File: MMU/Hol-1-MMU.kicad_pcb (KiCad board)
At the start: 2 copper layers, 106.7 x 76.2 mm, 0 parts

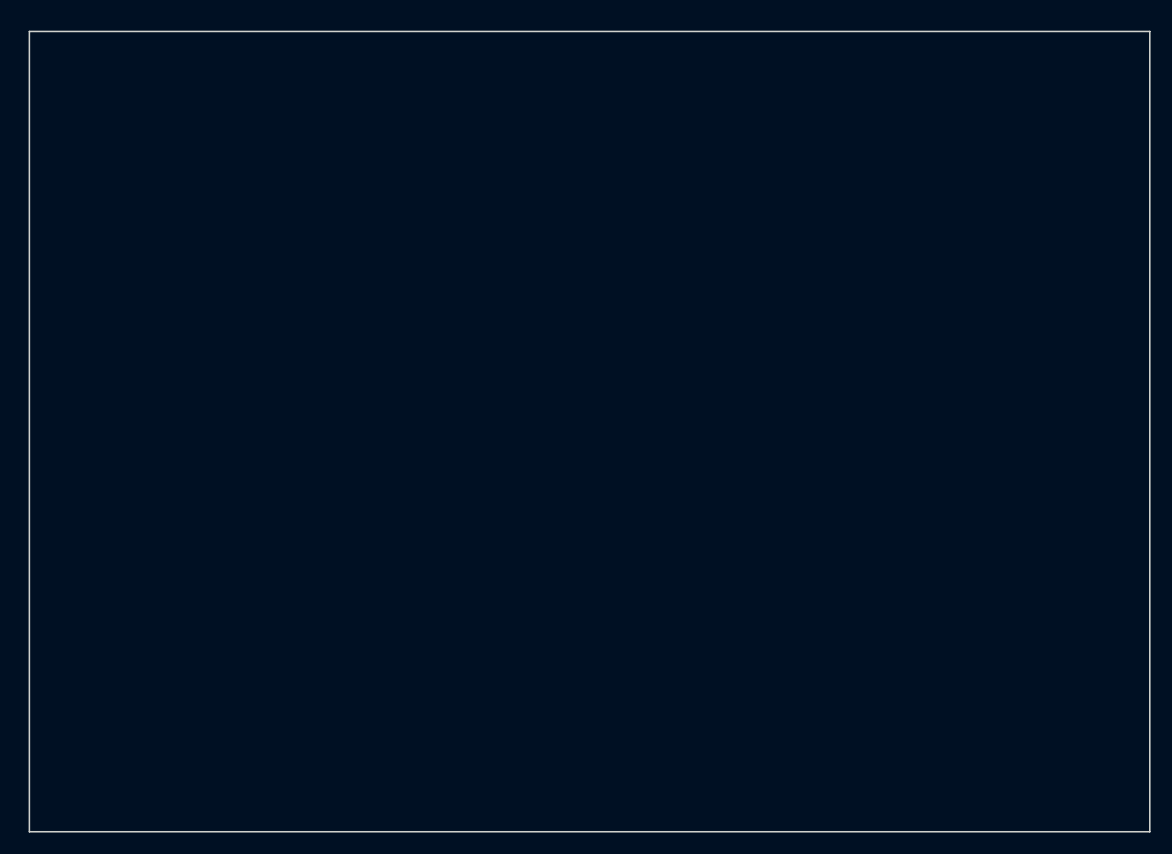
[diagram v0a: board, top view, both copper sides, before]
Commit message: v1.5.2 MMU power + blinkenlights added
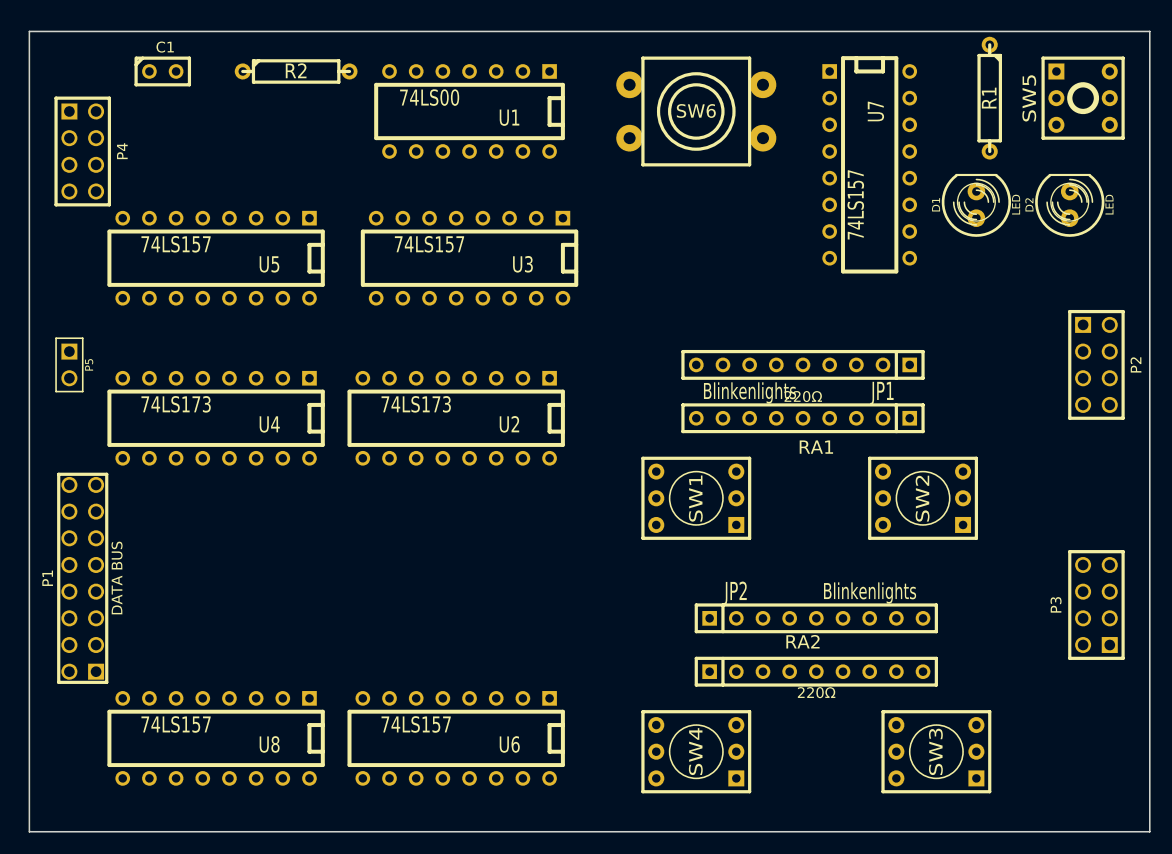
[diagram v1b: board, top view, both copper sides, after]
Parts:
- added C1: 0.01uF, C1, F.Cu at (116.8, 67.3)
- added D1: LED, LED-5MM, F.Cu at (194.3, 80.0)
- added D2: LED, LED-5MM, F.Cu at (203.2, 80.0)
- added JP1: Blinkenlights, SIL-9, F.Cu at (177.8, 95.2)
- added JP2: Blinkenlights, SIL-9, F.Cu at (179.1, 119.4)
- added P1: DATA BUS, pin_array_8x2, F.Cu at (109.2, 115.6)
- added P2: ADDRESS PORT, pin_array_4x2, F.Cu at (205.7, 95.2)
- added P3: DATA PORT, pin_array_4x2, F.Cu at (205.7, 118.1)
- added P4: MMU CONTROL, pin_array_4x2, F.Cu at (109.2, 74.9)
- added P5: Power, PIN_ARRAY_2X1, F.Cu at (108.0, 95.2)
- added R1: 220Ω, R4, F.Cu at (195.6, 69.8)
- added R2: 1K, R4, F.Cu at (129.5, 67.3)
- added RA1: 220Ω, r_pack8, F.Cu at (177.8, 100.3)
- added RA2: 220Ω, r_pack8, F.Cu at (179.1, 124.5)
- added SW1: HEX_SWITCH, SW_Hex6, F.Cu at (167.6, 108.0)
- added SW2: HEX_SWITCH, SW_Hex6, F.Cu at (189.2, 108.0)
- added SW3: HEX_SWITCH, SW_Hex6, F.Cu at (190.5, 132.1)
- added SW4: HEX_SWITCH, SW_Hex6, F.Cu at (167.6, 132.1)
- added SW5: DPDT, sw-dpdt-push, F.Cu at (204.5, 69.8)
- added SW6: SW_PUSH, sw_push_lrg, F.Cu at (167.6, 71.1)
- added U1: 74LS00, DIP-14, F.Cu at (146.1, 71.1)
- added U2: 74LS173, DIP-16, F.Cu at (144.8, 100.3)
- added U3: 74LS157, DIP-16, F.Cu at (146.1, 85.1)
- added U4: 74LS173, DIP-16, F.Cu at (121.9, 100.3)
- added U5: 74LS157, DIP-16, F.Cu at (121.9, 85.1)
- added U6: 74LS157, DIP-16, F.Cu at (144.8, 130.8)
- added U7: 74LS157, DIP-16, F.Cu at (184.2, 76.2)
- added U8: 74LS157, DIP-16, F.Cu at (121.9, 130.8)

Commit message: v1.5.3 initial MMU board layout
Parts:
- moved P2 79.1 mm to (130.8, 69.8), turned to 180 degrees
- moved SW5 58.8 mm to (172.7, 119.4), turned to 180 degrees
- moved D2 46.6 mm to (162.6, 102.9)
- moved R1 44.7 mm to (170.2, 106.7), turned to 0 degrees
- moved P3 44.5 mm to (161.3, 118.1)
- moved SW4 42.1 mm to (204.5, 111.8)
- moved SW1 40.4 mm to (204.5, 91.4)
- moved SW2 39.9 mm to (204.5, 71.1)
- moved D1 28.2 mm to (177.8, 102.9)
- moved RA1 22.5 mm to (193.0, 83.8), turned to 270 degrees
- moved U7 20.4 mm to (163.8, 74.9)
- moved RA2 14.9 mm to (193.0, 119.4), turned to 270 degrees
- moved SW3 14.0 mm to (204.5, 132.1)
- moved JP1 12.5 mm to (182.9, 83.8), turned to 270 degrees
- moved SW6 7.73 mm to (175.3, 72.4), turned to 270 degrees
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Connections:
- P4 pad 1: /RAM-INPUT -> (no net)
- P4 pad 2: /CLK -> (no net)
- P4 pad 4: (no net) -> /RAM-INPUT
- P4 pad 6: (no net) -> /CLK
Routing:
- net GND: track 0.00 -> 375.7 mm, vias 0 -> 15
- net +5V: track 0.00 -> 360.7 mm, vias 0 -> 8
- net /PROG: track 0.00 -> 162.3 mm, vias 0 -> 4
- net N-0000049: track 0.00 -> 119.5 mm, vias 0 -> 3
- net N-0000050: track 0.00 -> 117.9 mm, vias 0 -> 4
- net N-0000010: track 0.00 -> 110.3 mm, vias 0 -> 3
- net N-000006: track 0.00 -> 109.5 mm, vias 0 -> 2
- net N-0000056: track 0.00 -> 106.7 mm, vias 0 -> 1
- net N-000002: track 0.00 -> 102.7 mm
- net N-0000062: track 0.00 -> 99.4 mm, vias 0 -> 4
- net N-0000063: track 0.00 -> 92.0 mm, vias 0 -> 4
- net N-000003: track 0.00 -> 87.4 mm, vias 0 -> 1
- net N-000001: track 0.00 -> 79.0 mm, vias 0 -> 2
- net N-0000064: track 0.00 -> 78.0 mm, vias 0 -> 2
- net N-0000040: track 0.00 -> 78.0 mm, vias 0 -> 1
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
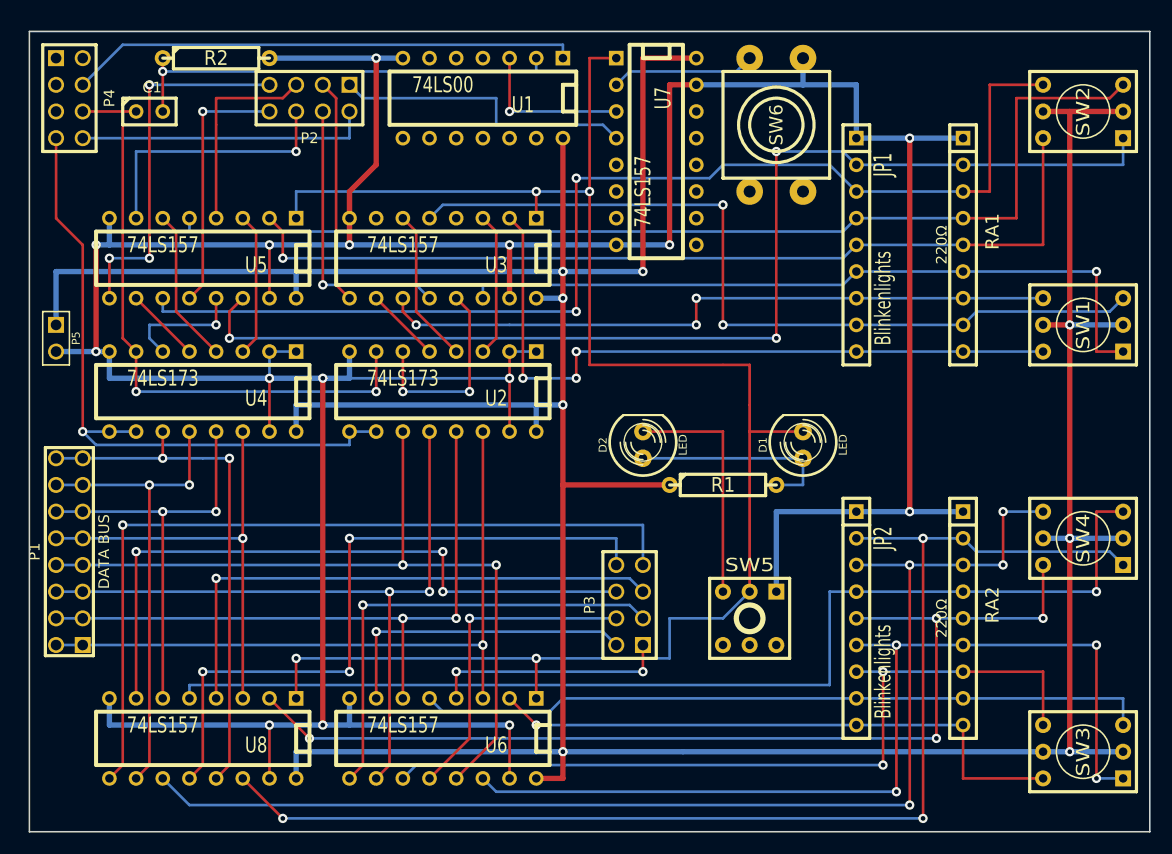
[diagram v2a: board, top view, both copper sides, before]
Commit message: v1.5.4 MMU add bypass caps
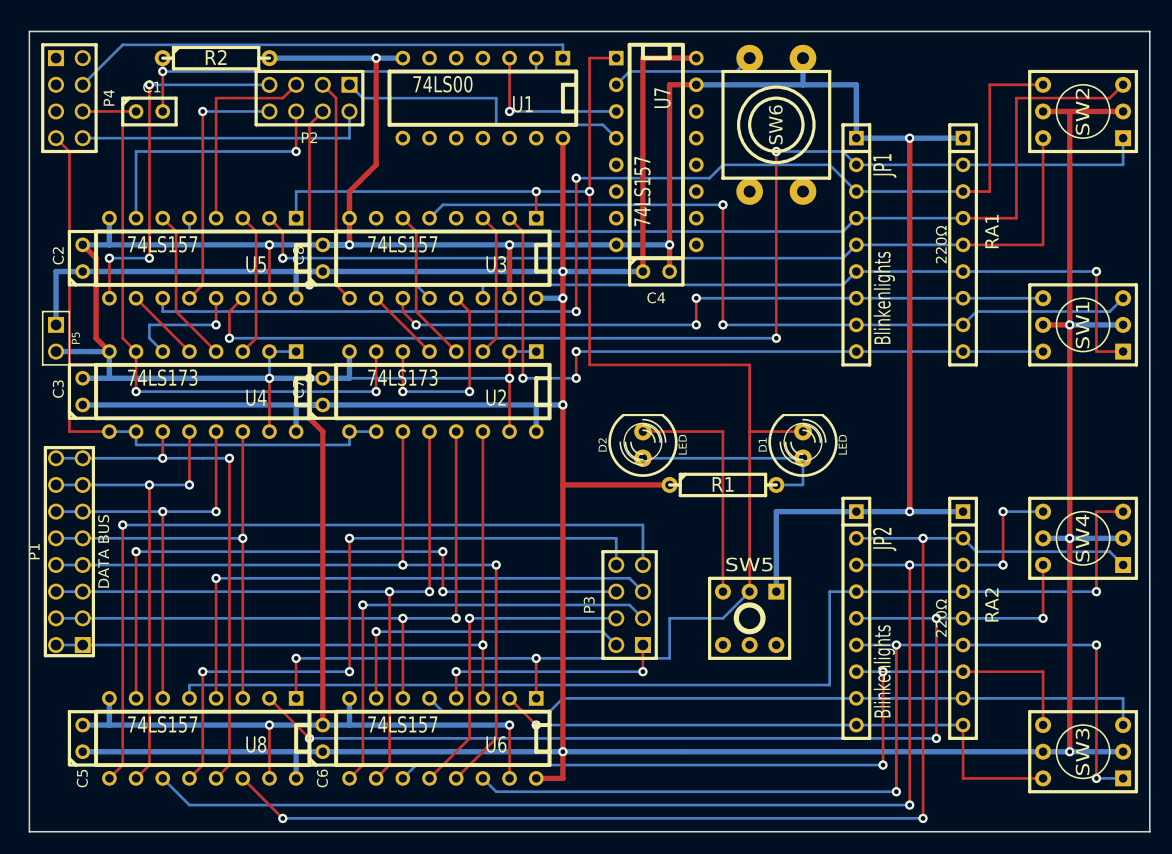
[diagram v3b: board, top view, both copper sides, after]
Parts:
- added C2: 100nF, C1, F.Cu at (109.2, 85.1)
- added C3: 100nF, C1, F.Cu at (109.2, 97.8)
- added C4: 100nF, C1, F.Cu at (163.8, 86.4)
- added C5: 100nF, C1, F.Cu at (109.2, 130.8)
- added C6: 100nF, C1, F.Cu at (132.1, 130.8)
- added C7: 100nF, C1, F.Cu at (132.1, 97.8)
- added C8: 100nF, C1, F.Cu at (132.1, 85.1)
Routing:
- net +5V: track 360.7 -> 405.1 mm, vias 8 -> 7
- net GND: track 375.7 -> 388.7 mm, vias 15 -> 12
- net /IN-D: track 63.8 -> 60.2 mm, vias 1 -> 0
- net N-0000018: track 27.2 -> 29.0 mm

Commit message: v1.5.5 MMU reduce vias and tidy-up
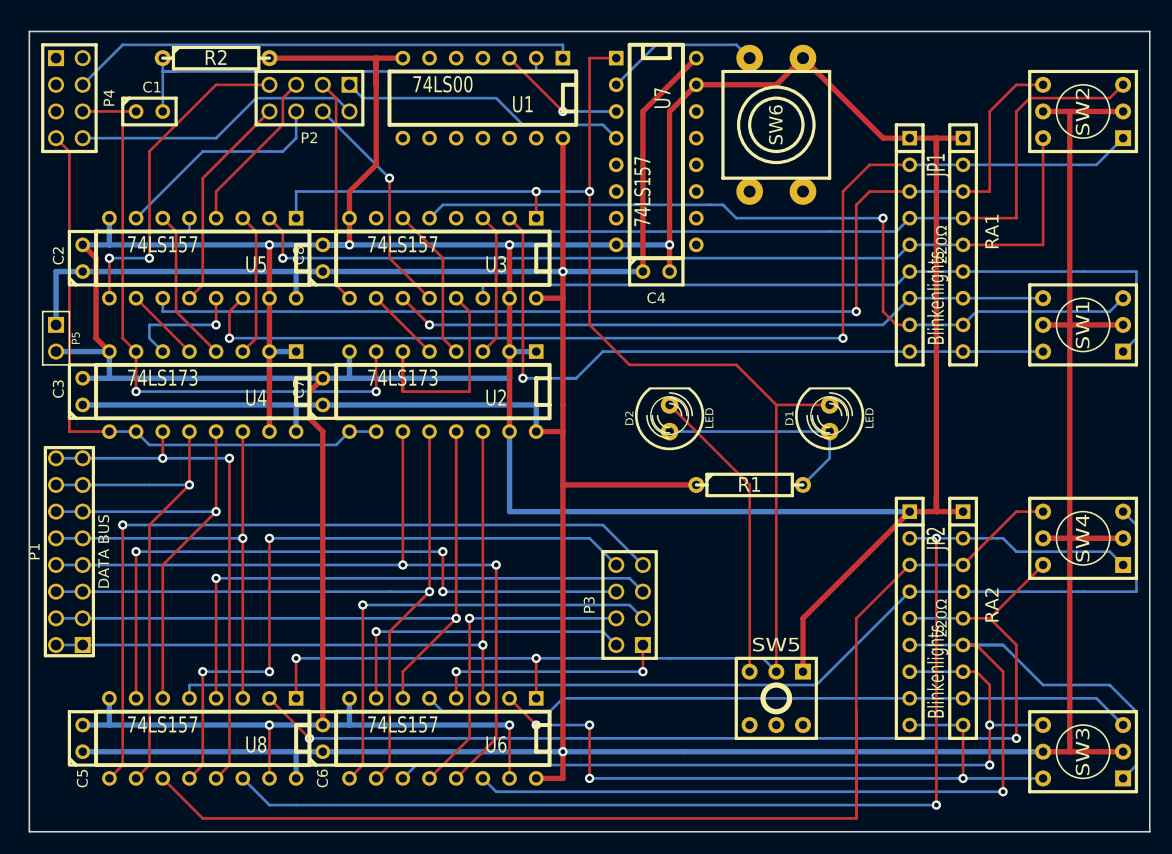
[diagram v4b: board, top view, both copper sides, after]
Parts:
- moved SW5 8.03 mm to (175.3, 127.0)
- moved JP1 5.08 mm to (188.0, 83.8)
- moved JP2 5.08 mm to (188.0, 119.4)
- moved D1 3.59 mm to (180.3, 100.3)
- moved D2 3.59 mm to (165.1, 100.3)
- moved R1 2.54 mm to (172.7, 106.7)
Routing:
- net GND: track 388.7 -> 449.5 mm, vias 12 -> 6
- net N-0000041: track 56.9 -> 67.1 mm, vias 1 -> 4
- net N-0000051: track 92.0 -> 101.3 mm, vias 4 -> 1
- net N-0000018: track 29.0 -> 22.0 mm
- net N-0000011: track 22.9 -> 28.6 mm
- net N-0000047: track 119.5 -> 113.9 mm, vias 3 -> 2
- net N-0000023: track 109.5 -> 104.4 mm, vias 2 -> 1
- net N-0000022: track 110.3 -> 105.5 mm, vias 3 -> 2
- net N-0000016: track 25.4 -> 20.9 mm, vias 1 -> 0
- net /PROG: track 162.3 -> 166.2 mm
- net N-0000030: track 19.6 -> 23.4 mm, vias 2 -> 0
- net N-0000015: track 35.6 -> 31.8 mm, vias 3 -> 2
- net N-0000017: track 19.6 -> 15.9 mm
- net N-0000014: track 24.7 -> 20.9 mm, vias 1 -> 0
- net N-0000046: track 106.7 -> 103.3 mm, vias 1 -> 0
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
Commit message: v1.5.6 MMU 10-pin jumpers for hex display blinkenlights
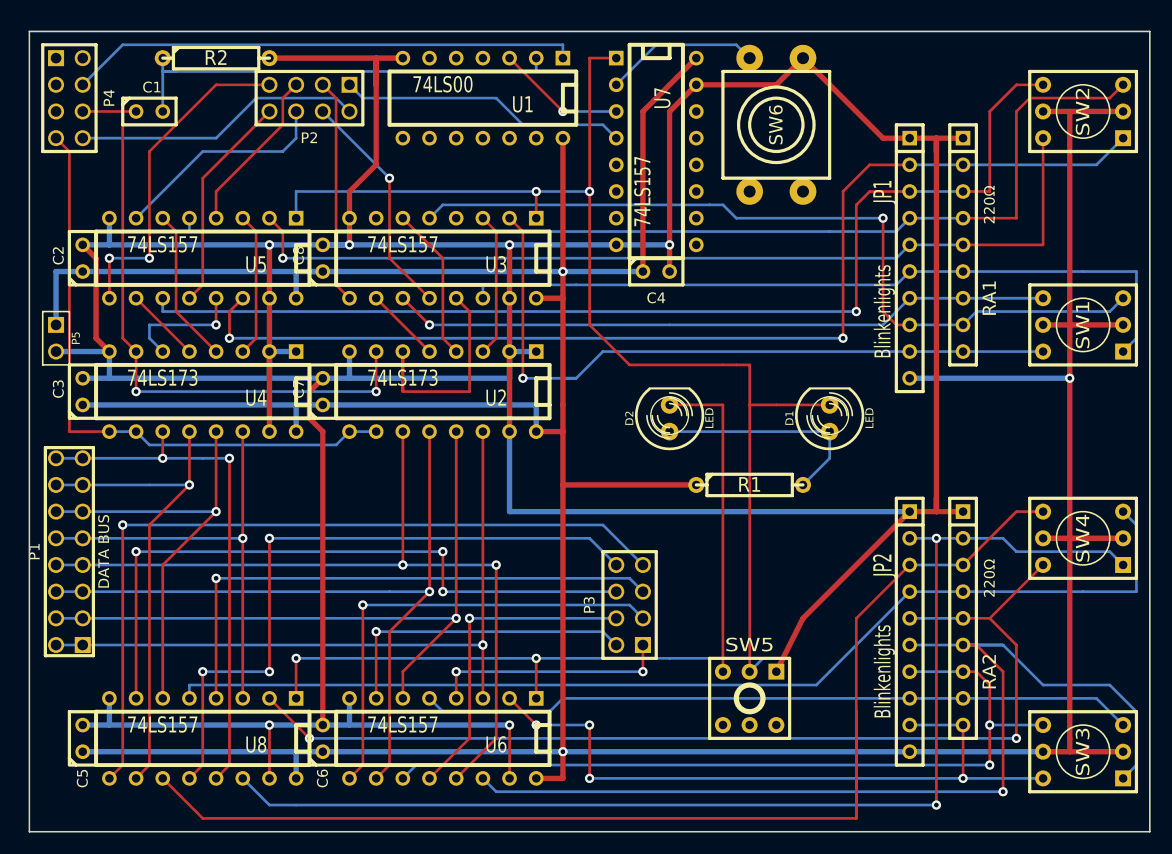
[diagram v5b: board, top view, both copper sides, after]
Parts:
- JP1, JP2: footprint SIL-9 -> SIL-10
- moved SW5 2.54 mm to (172.7, 127.0)
- moved JP1 1.27 mm to (188.0, 85.1)
- moved JP2 1.27 mm to (188.0, 120.7)
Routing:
- net +5V: track 402.2 -> 417.4 mm, vias 2 -> 3
- net /PROG: track 166.2 -> 168.5 mm
- net N-000009: track 28.6 -> 30.5 mm
- net GND: track 449.5 -> 450.1 mm

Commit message: v1.5.7 MMU more ergonomic layout for data input
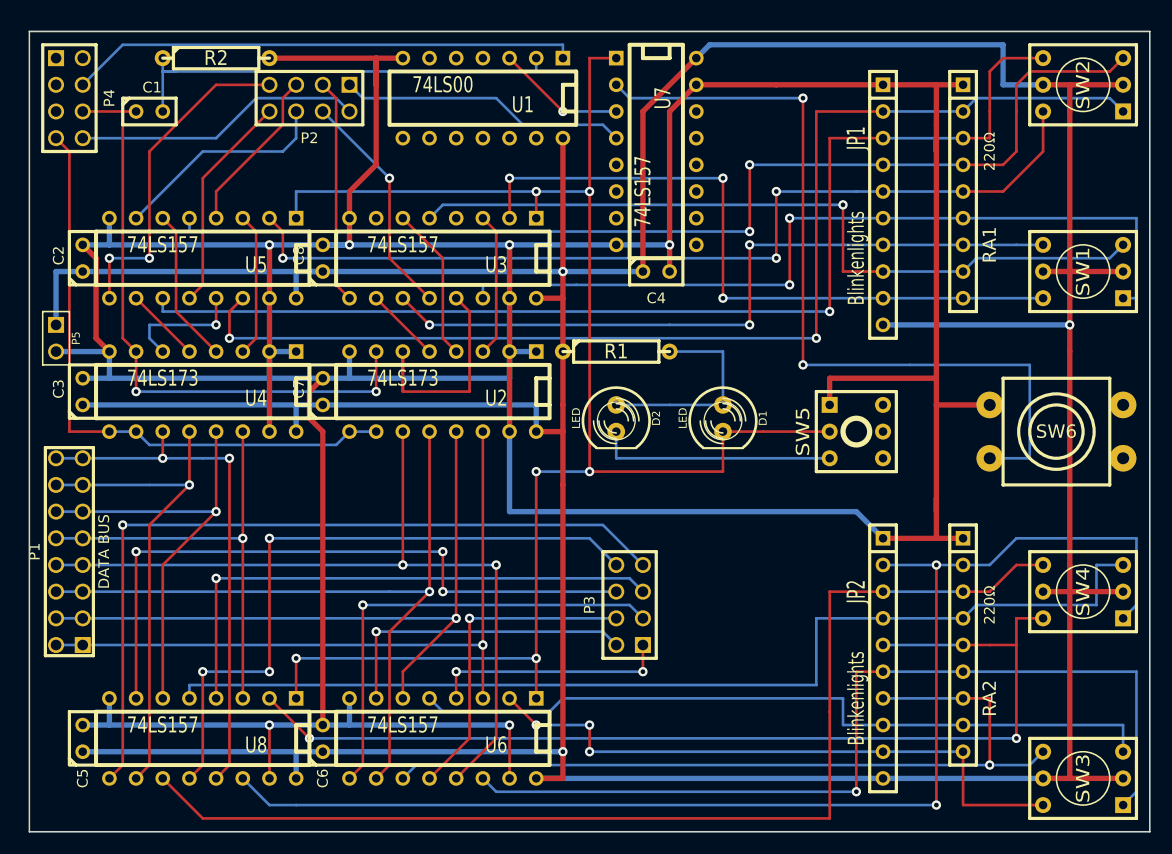
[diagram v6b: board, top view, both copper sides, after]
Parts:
- moved SW6 39.6 mm to (201.9, 101.6), turned to 0 degrees
- moved SW5 27.4 mm to (182.9, 101.6), turned to 270 degrees
- moved R1 18.0 mm to (160.0, 94.0)
- moved D1 10.2 mm to (170.2, 100.3), turned to 270 degrees
- moved JP1 5.68 mm to (185.4, 80.0)
- moved RA1 5.08 mm to (193.0, 78.7)
- moved SW1 5.08 mm to (204.5, 86.4)
- moved SW4 5.08 mm to (204.5, 116.8)
- moved D2 5.08 mm to (160.0, 100.3), turned to 270 degrees
- moved JP2 3.59 mm to (185.4, 123.2)
- moved RA2 2.54 mm to (193.0, 121.9)
- moved SW2 2.54 mm to (204.5, 68.6)
- moved SW3 2.54 mm to (204.5, 134.6)
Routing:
- net N-0000057: track 14.8 -> 78.0 mm, vias 0 -> 2
- net +5V: track 417.4 -> 452.2 mm
- net N-0000021: track 101.3 -> 87.4 mm
- net /PROG: track 168.5 -> 154.9 mm, vias 4 -> 6
- net N-0000018: track 118.8 -> 108.0 mm
- net N-0000017: track 113.9 -> 123.3 mm
- net N-000009: track 30.5 -> 22.9 mm
- net N-0000011: track 67.1 -> 59.5 mm, vias 4 -> 3
- net N-0000043: track 63.1 -> 69.6 mm, vias 1 -> 3
- net N-0000042: track 72.2 -> 78.7 mm, vias 0 -> 2
- net N-0000039: track 105.5 -> 112.1 mm
- net N-0000040: track 104.4 -> 108.5 mm
- net N-0000015: track 68.1 -> 72.2 mm
- net N-0000044: track 77.6 -> 74.0 mm
- net GND: track 450.1 -> 453.6 mm
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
